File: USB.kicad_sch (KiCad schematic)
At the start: 34 parts, among them J1 USB_C_Receptable_USB2.0, U1 AP2141WG-7

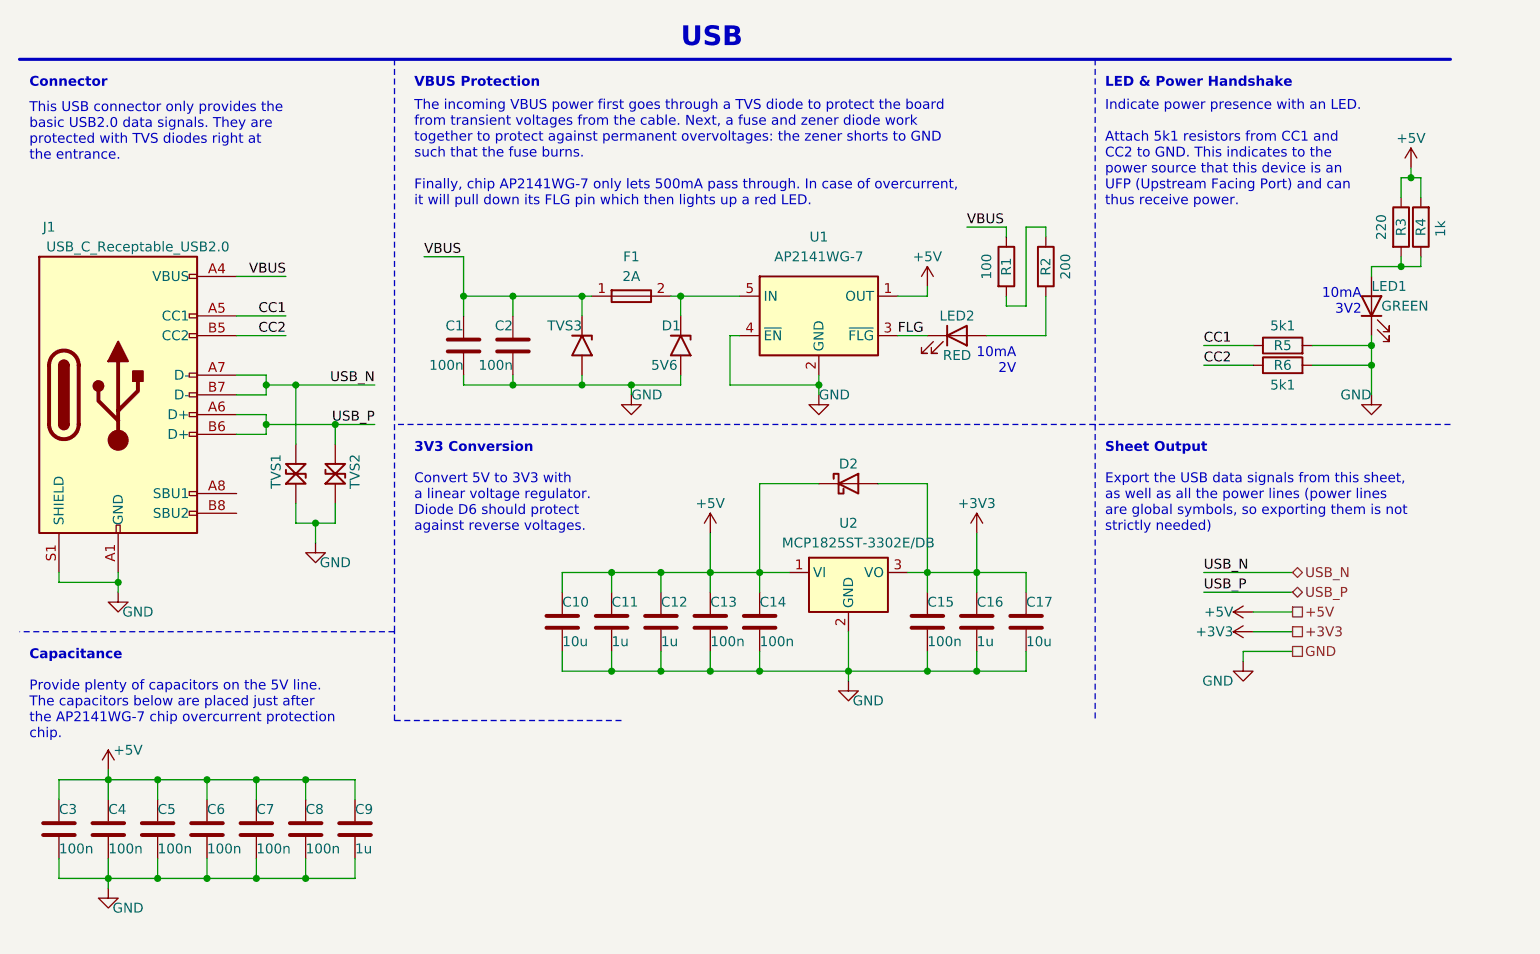
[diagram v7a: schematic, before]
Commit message: Prefix each symbol name in library - eg. 'D_', 'CONN_', 'IC_', ...
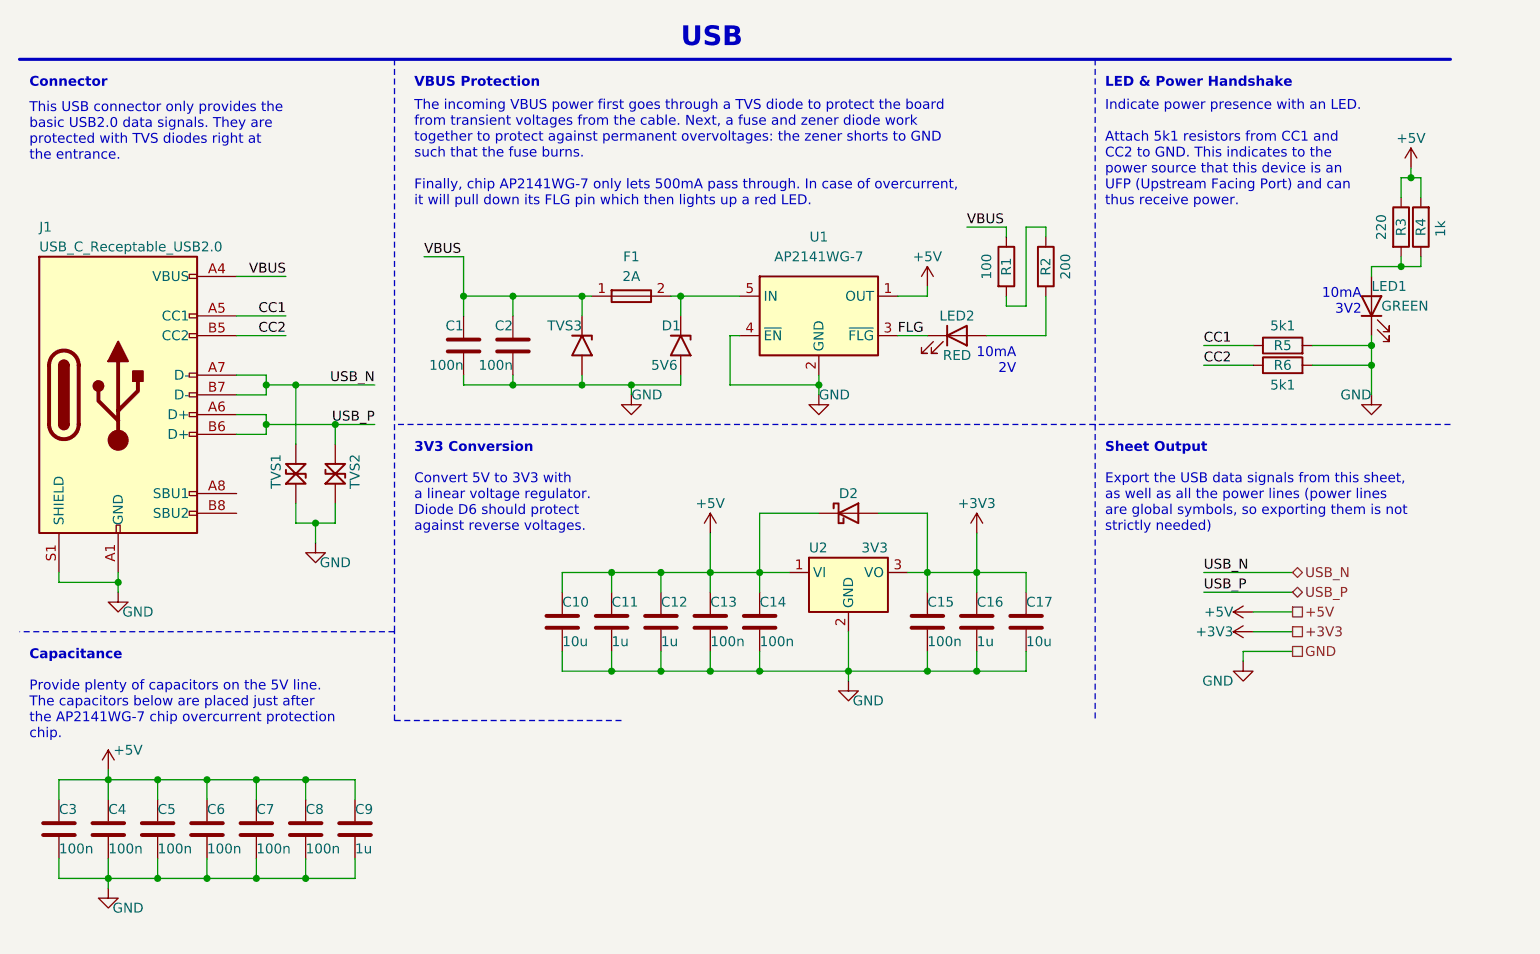
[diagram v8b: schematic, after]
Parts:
- D2: value ~ -> 40V 350mA; symbol Tiny_Scarab:SD103AWS -> Tiny_Scarab:D_SCHOTTKY_SD103AWS; SPN 4530-SD103AWSTR-ND -> (none); Supplier DigiKey -> (none)
- J1: symbol Tiny_Scarab:USB_C_Receptable_USB2.0 -> Tiny_Scarab:CONN_USB_C_RECEPTABLE_USB2.0
- TVS1, TVS2: symbol Tiny_Scarab:CDSOD323-T05LC -> Tiny_Scarab:TVS_CDSOD323-T05LC
- U1: symbol Tiny_Scarab:AP2141WG-7 -> Tiny_Scarab:IC_AP2141WG-7
- U2: value ~ -> 3V3; symbol Tiny_Scarab:MCP1825ST-3302E/DB -> Tiny_Scarab:IC_MCP1825ST-3302E-DB; SPN MCP1825ST-3302E/DBTR-ND -> (none); Supplier DigiKey -> (none)
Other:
- moved on the sheet: D2
